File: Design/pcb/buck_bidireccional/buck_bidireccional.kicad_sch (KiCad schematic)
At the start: 19 parts, among them J1 Conn_01x02_Pin, J2 Screw_Terminal_01x02, J3 Screw_Terminal_01x02, J4 Conn_01x02_Pin, Q1 NMOS, Q2 NMOS, U1 IR2184

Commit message: updated pcb
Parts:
- removed C1: 6.8u, Capacitor_THT:CP_Radial_D5.0mm_P2.00mm, symbol Device:C
- removed C2: 2.2u, Capacitor_THT:CP_Radial_D5.0mm_P2.00mm, symbol Device:C
- added C1: 6.8u, Capacitor_THT:CP_Radial_D5.0mm_P2.00mm, symbol Device:C_Polarized
- added C2: 2.2u, Capacitor_THT:CP_Radial_D5.0mm_P2.00mm, symbol Device:C_Polarized
- added C4: 4.7u, Capacitor_THT:CP_Radial_D5.0mm_P2.00mm, symbol Device:C
- added J5: Screw_Terminal_01x02, TerminalBlock_Phoenix:TerminalBlock_Phoenix_MKDS-1,5-2-5.08_1x02_P5.08mm_Horizontal, symbol Connector:Screw_Terminal_01x02
- added R6: 10k, Resistor_THT:R_Axial_DIN0207_L6.3mm_D2.5mm_P7.62mm_Horizontal, symbol Device:R
- R4, R5: value 100k -> 10k
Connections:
- net +12V: now also J5.1 (Pin_1)
- net GND: now also C1.2, C2.2, J5.2 (Pin_2), R6.2
- net at J2.1 (Pin_1), J4.1 (Pin_1), L1.1: now also C2.1
- net at C3.2, J4.2 (Pin_2), L1.2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: now also C4.2
- net at J1.1 (Pin_1), U1.1 (IN): now also R6.1
- net at J3.1 (Pin_1), Q1.1 (D): now also C1.1
- net at D2.1 (K), R3.1, U1.7 (HO): now also C4.1

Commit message: updates kiskas
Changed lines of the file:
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@@
 (kicad_sch
-	(version 20231120)
+	(version 20250114)
 	(generator "eeschema")
-	(generator_version "8.0")
+	(generator_version "9.0")
 	(paper "A4")
+	(text_box "Footprints \n\nterminal block:	TerminalBlock_Phoenix:TerminalBlock_Phoenix_MKDS-1,5-2-5.08_1x02_P5.08mm_Horizontal \ncapacitors:  Capacitor_THT:CP_Radial_D5.0mm_P2.00mm \nresistors: R_Axial_DIN0207_L6.3mm_D2.5mm_P7.62mm_Horizontal (REVISION)\ndiodes: Diode_THT:D_A-405_P7.62mm_Horizontal(REVISION)\nmosfets: TO-220-3_Vertical\npins:	Connector_PinHeader_2.54mm:PinHeader_1x02_P2.54mm_Vertical\ndriver:	Package_DIP:DIP-8_W7.62mm"
+		(exclude_from_sim no)
+		(at 177.8 19.05 0)
+		(size 104.14 22.86)
+		(margins 0.9525 0.9525 0.9525 0.9525)
+		(stroke
+			(width 0)
+			(type default)
+		)
+		(fill
+			(type none)
+		)
+		(effects
+			(font
+				(size 1.27 1.27)
+			)
+			(justify left top)
+		)
+	)
 	(junction
 		(at 127 92.71)
@@
 			(width 0)
 			(type default)
-		)
-	)
-	(text_box "Footprints \n\nterminal block:	TerminalBlock_Phoenix:TerminalBlock_Phoenix_MKDS-1,5-2-5.08_1x02_P5.08mm_Horizontal \ncapacitors:  Capacitor_THT:CP_Radial_D5.0mm_P2.00mm \nresistors: R_Axial_DIN0207_L6.3mm_D2.5mm_P7.62mm_Horizontal (REVISION)\ndiodes: Diode_THT:D_A-405_P7.62mm_Horizontal(REVISION)\nmosfets: TO-220-3_Vertical\npins:	Connector_PinHeader_2.54mm:PinHeader_1x02_P2.54mm_Vertical\ndriver:	Package_DIP:DIP-8_W7.62mm"
-		(exclude_from_sim no)
-		(at 177.8 19.05 0)
-		(size 104.14 22.86)
-		(stroke
-			(width 0)
-			(type default)
-		)
-		(fill
-			(type none)
-		)
-		(effects
-			(font
-				(size 1.27 1.27)
-			)
-			(justify left top)
 		)
 	)
@@
 		)
 	)
+	(embedded_fonts no)
 )

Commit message: update kicad
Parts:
- C4: value 4.7u -> 100n
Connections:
- net +12V: now also C4.1
- net GND: now also C4.2
- net at C3.2, J4.2 (Pin_2), L1.2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: no longer C4.2
- net at D2.1 (K), R3.1, U1.7 (HO): no longer C4.1
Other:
- moved on the sheet: J5

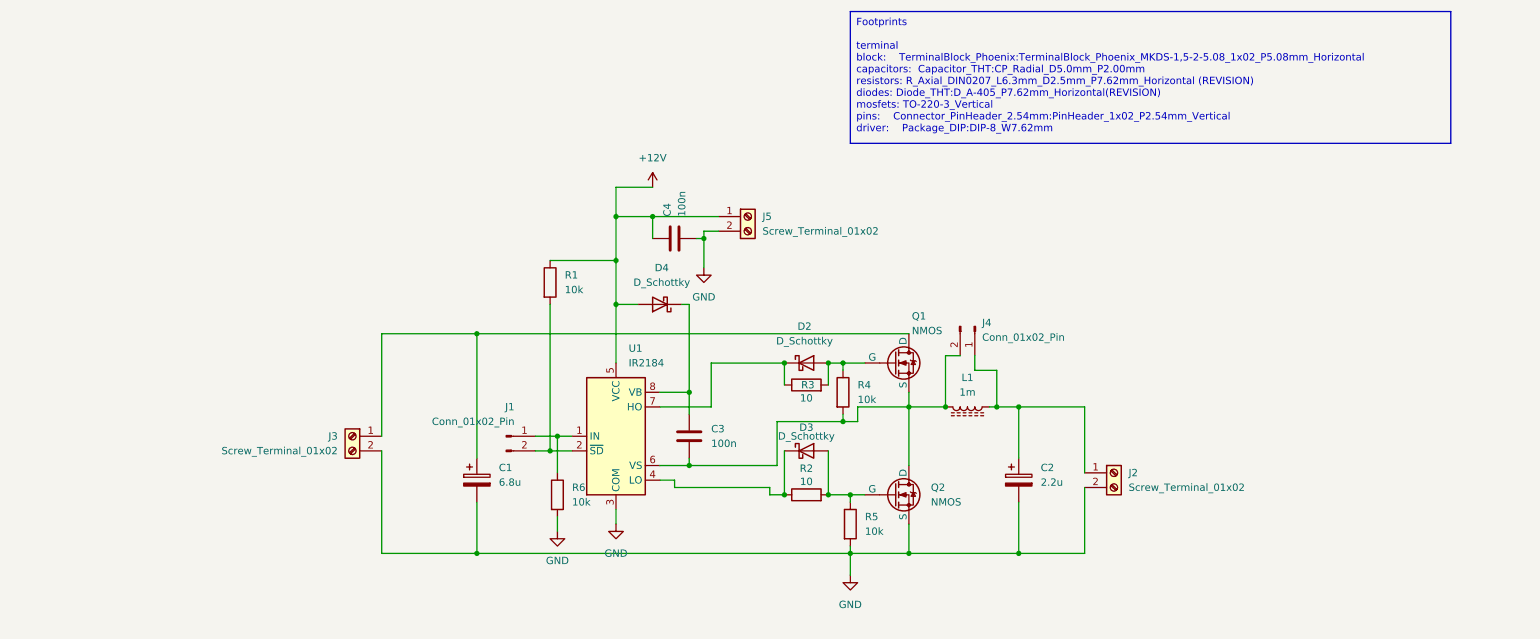
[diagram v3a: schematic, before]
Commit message: updated kicad
MOSFET gate oscilloscope reading still missing
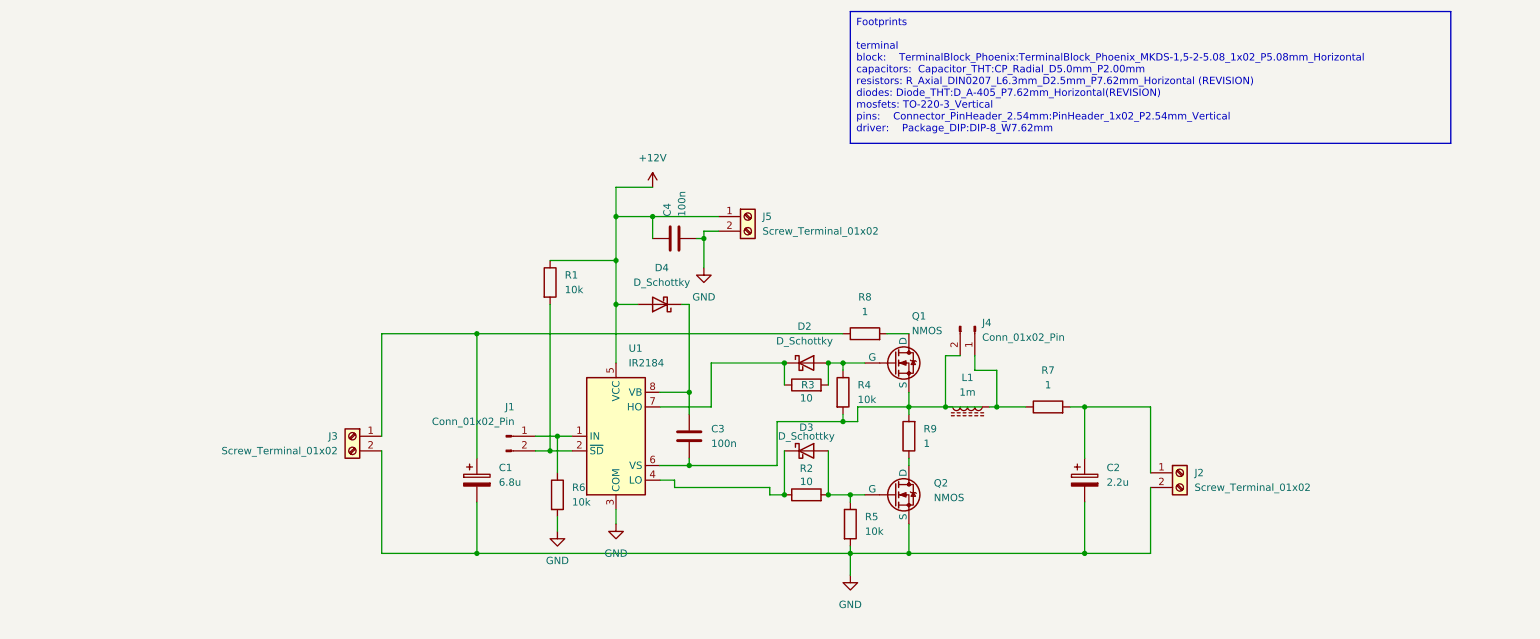
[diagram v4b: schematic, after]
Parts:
- added R7, R8, R9: 1, Resistor_THT:R_Axial_DIN0207_L6.3mm_D2.5mm_P7.62mm_Horizontal, symbol Device:R
- U1: footprint Package_DIP:DIP-8_W7.62mm -> Package_SO:SOIC-8_3.9x4.9mm_P1.27mm
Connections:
- net at J4.1 (Pin_1), L1.1: now also R7.1; no longer C2.1, J2.1 (Pin_1)
- net at C3.2, J4.2 (Pin_2), L1.2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: now also R9.2; no longer Q2.1 (D)
- net at C1.1, J3.1 (Pin_1): now also R8.1; no longer Q1.1 (D)
- new net: Q2.1 (D), R9.1
- new net: C2.1, J2.1 (Pin_1), R7.2
- new net: Q1.1 (D), R8.2
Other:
- moved on the sheet: C2, J2

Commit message: final kicad
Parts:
- removed R7, R8, R9: 1, Resistor_THT:R_Axial_DIN0207_L6.3mm_D2.5mm_P7.62mm_Horizontal, symbol Device:R
- added DQ1, DQ2, IL1: TestPoint, TestPoint:TestPoint_Bridge_Pitch2.54mm_Drill0.7mm, symbol Connector:TestPoint
- added Vgs_Q1, Vgs_Q2: Conn_01x02_Pin, Connector_PinHeader_2.54mm:PinHeader_1x02_P2.54mm_Vertical, symbol Connector:Conn_01x02_Pin
- renumbered J1 to PWM1, J5 to Vcc1, J4 to Vl1
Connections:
- net GND: now also Vgs_Q2.1 (Pin_1)
- net at L1.1, Vl1.1 (Pin_1): now also C2.1, J2.1 (Pin_1), IL1.1
- net VS: now reaches C3.2, L1.2, Q1.3 (S), R4.2, U1.6 (VS), Vl1.2 (Pin_2)
- net VS: now also Q2.1 (D), DQ2.1, Vgs_Q1.1 (Pin_1)
- net LO: now reaches D3.2 (A), Q2.2 (G), R2.2, R5.1
- net LO: now also Vgs_Q2.2 (Pin_2)
- net HO: now reaches D2.2 (A), Q1.2 (G), R3.2, R4.1
- net HO: now also Vgs_Q1.2 (Pin_2)
- net at C1.1, J3.1 (Pin_1): now also Q1.1 (D), DQ1.1
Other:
- moved on the sheet: C1, C2, C3, C4, D2, D3, D4, J2, J3, L1, PWM1, Q1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

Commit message: final pcb
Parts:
- L1: footprint BUCK_INDUCTOR:buck_inductor -> inductores:buck_inductor
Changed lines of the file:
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@@
 	)
 	(junction
-		(at 81.28 68.58)
+		(at 184.15 88.9)
 		(diameter 0)
 		(color 0 0 0 0)
 	)
 	(junction
-		(at 184.15 88.9)
+		(at 81.28 68.58)
 		(diameter 0)
 		(color 0 0 0 0)
@@
 	(wire
 		(pts
-			(xy 207.01 88.9) (xy 200.66 88.9)
-		)
-		(stroke
-			(width 0)
-			(type default)
-		)
-	)
-	(wire
-		(pts
 			(xy 184.15 104.14) (xy 184.15 105.41)
 		)
@@
 	(wire
 		(pts
-			(xy 236.22 102.87) (xy 236.22 114.3)
+			(xy 81.28 69.85) (xy 81.28 68.58)
 		)
 		(stroke
@@
 	(wire
 		(pts
-			(xy 184.15 72.39) (xy 184.15 78.74)
+			(xy 236.22 102.87) (xy 236.22 114.3)
 		)
 		(stroke
@@
 	(wire
 		(pts
-			(xy 184.15 104.14) (xy 186.69 104.14)
+			(xy 184.15 72.39) (xy 184.15 78.74)
 		)
 		(stroke
@@
 	(wire
 		(pts
-			(xy 224.79 105.41) (xy 224.79 114.3)
+			(xy 184.15 104.14) (xy 186.69 104.14)
 		)
 		(stroke
@@
 	(wire
 		(pts
-			(xy 66.04 118.11) (xy 66.04 115.57)
+			(xy 224.79 105.41) (xy 224.79 114.3)
 		)
 		(stroke
@@
 	(wire
 		(pts
-			(xy 92.71 95.25) (xy 92.71 92.71)
+			(xy 66.04 118.11) (xy 66.04 115.57)
 		)
 		(stroke
@@
 	(wire
 		(pts
-			(xy 78.74 99.06) (xy 78.74 95.25)
+			(xy 92.71 95.25) (xy 92.71 92.71)
 		)
 		(stroke
@@
 	(wire
 		(pts
-			(xy 81.28 73.66) (xy 81.28 68.58)
+			(xy 78.74 99.06) (xy 78.74 95.25)
 		)
 		(stroke
@@
 			)
 		)
-		(property "Footprint" "BUCK_INDUCTOR:buck_inductor"
+		(property "Footprint" "inductores:buck_inductor"
 			(at 204.47 88.9 0)
 			(effects
@@
 	(symbol
 		(lib_id "power:GND")
-		(at 81.28 73.66 0)
+		(at 66.04 118.11 0)
 		(unit 1)
 		(exclude_from_sim no)
@@
 		(dnp no)
 		(fields_autoplaced yes)
-		(property "Reference" "#PWR05"
-			(at 81.28 80.01 0)
+		(property "Reference" "#PWR02"
+			(at 66.04 124.46 0)
 			(effects
 				(font
@@
 		)
 		(property "Value" "GND"
-			(at 81.28 78.74 0)
+			(at 66.04 123.19 0)
 			(effects
 				(font
@@
 		)
 		(property "Footprint" ""
-			(at 81.28 73.66 0)
+			(at 66.04 118.11 0)
 			(effects
 				(font
@@
 		)
 		(property "Datasheet" ""
-			(at 81.28 73.66 0)
+			(at 66.04 118.11 0)
 			(effects
 				(font
@@
 		)
 		(property "Description" "Power symbol creates a global label with name \"GND\" , ground"
-			(at 81.28 73.66 0)
+			(at 66.04 118.11 0)
 			(effects
 				(font
@@
 			(project "buck_bidireccional"
 				(path "/a506e00b-eae2-41ca-a9b6-22a3d546bb26"
-					(reference "#PWR05")
+					(reference "#PWR02")
 					(unit 1)
 				)
@@
 	(symbol
 		(lib_id "power:GND")
-		(at 66.04 118.11 0)
+		(at 81.28 69.85 0)
 		(unit 1)
 		(exclude_from_sim no)
@@
 		(dnp no)
 		(fields_autoplaced yes)
-		(property "Reference" "#PWR02"
-			(at 66.04 124.46 0)
+		(property "Reference" "#PWR05"
+			(at 81.28 76.2 0)
 			(effects
 				(font
@@
 		)
 		(property "Value" "GND"
-			(at 66.04 123.19 0)
+			(at 81.28 74.93 0)
 			(effects
 				(font
@@
 		)
 		(property "Footprint" ""
-			(at 66.04 118.11 0)
+			(at 81.28 69.85 0)
 			(effects
 				(font
@@
 		)
 		(property "Datasheet" ""
-			(at 66.04 118.11 0)
+			(at 81.28 69.85 0)
 			(effects
 				(font
@@
 		)
 		(property "Description" "Power symbol creates a global label with name \"GND\" , ground"
-			(at 66.04 118.11 0)
+			(at 81.28 69.85 0)
 			(effects
 				(font
@@
 			(project "buck_bidireccional"
 				(path "/a506e00b-eae2-41ca-a9b6-22a3d546bb26"
-					(reference "#PWR02")
+					(reference "#PWR05")
 					(unit 1)
 				)

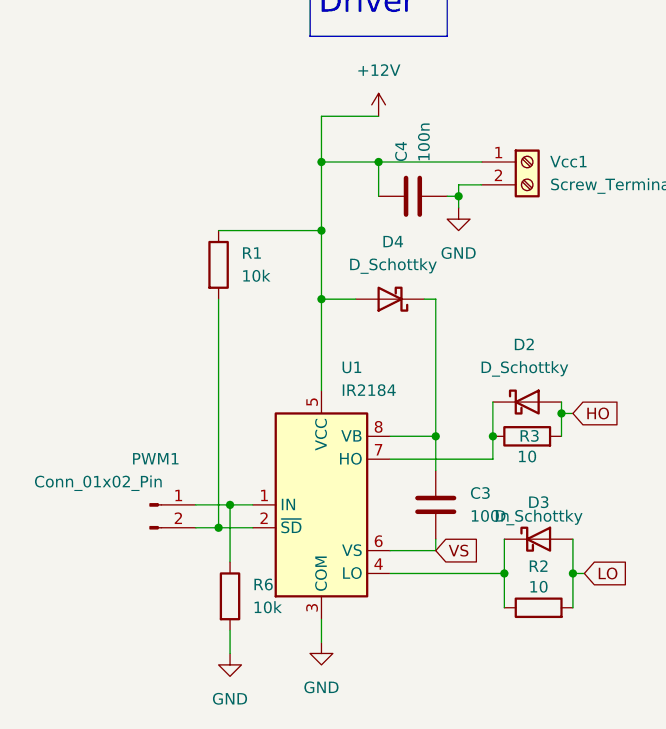
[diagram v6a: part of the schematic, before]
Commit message: removed non needed resistors
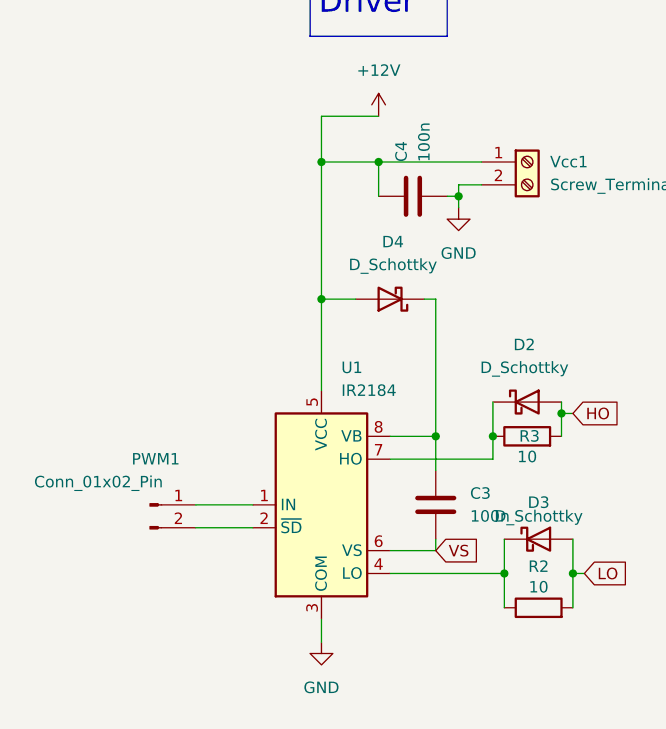
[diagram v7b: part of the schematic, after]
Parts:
- removed R1, R6: 10k, Resistor_THT:R_Axial_DIN0207_L6.3mm_D2.5mm_P7.62mm_Horizontal, symbol Device:R

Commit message: fixed kicad error
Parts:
- removed Vgs_Q1: Conn_01x02_Pin, Connector_PinHeader_2.54mm:PinHeader_1x02_P2.54mm_Vertical, symbol Connector:Conn_01x02_Pin
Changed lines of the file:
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@@
-	)
-	(junction
-		(at 189.23 88.9)
-		(diameter 0)
-		(color 0 0 0 0)
 	)
 	(junction
@@
 	)
 	(junction
-		(at 186.69 72.39)
-		(diameter 0)
-		(color 0 0 0 0)
-	)
-	(junction
 		(at 154.94 76.2)
 		(diameter 0)
@@
 	(wire
 		(pts
-			(xy 189.23 63.5) (xy 189.23 88.9)
-		)
-		(stroke
-			(width 0)
-			(type default)
-		)
-	)
-	(wire
-		(pts
 			(xy 73.66 110.49) (xy 86.36 110.49)
 		)
@@
 	(wire
 		(pts
-			(xy 184.15 88.9) (xy 189.23 88.9)
+			(xy 184.15 88.9) (xy 194.31 88.9)
 		)
 		(stroke
@@
 	(wire
 		(pts
-			(xy 189.23 88.9) (xy 194.31 88.9)
-		)
-		(stroke
-			(width 0)
-			(type default)
-		)
-	)
-	(wire
-		(pts
 			(xy 66.04 64.77) (xy 72.39 64.77)
 		)
@@
 		(pts
 			(xy 184.15 113.03) (xy 184.15 114.3)
-		)
-		(stroke
-			(width 0)
-			(type default)
-		)
-	)
-	(wire
-		(pts
-			(xy 186.69 63.5) (xy 186.69 72.39)
 		)
 		(stroke
@@
 					(unit 1)
 				)
-			)
-		)
-	)
-	(symbol
-		(lib_id "Connector:Conn_01x02_Pin")
-		(at 189.23 58.42 270)
-		(unit 1)
-		(exclude_from_sim no)
-		(in_bom yes)
-		(on_board yes)
-		(dnp no)
-		(property "Reference" "Vgs_Q1"
-			(at 177.038 62.23 90)
-			(effects
-				(font
-					(size 1.27 1.27)
-				)
-				(justify left)
-			)
-		)
-		(property "Value" "Conn_01x02_Pin"
-			(at 181.864 55.626 90)
-			(effects
-				(font
-					(size 1.27 1.27)
-				)
-				(justify left)
-			)
-		)
-		(property "Footprint" "Connector_PinHeader_2.54mm:PinHeader_1x02_P2.54mm_Vertical"
-			(at 189.23 58.42 0)
-			(effects
-				(font
-					(size 1.27 1.27)
-				)
-				(hide yes)
-			)
-		)
-		(property "Datasheet" "~"
-			(at 189.23 58.42 0)
-			(effects
-				(font
-					(size 1.27 1.27)
-				)
-				(hide yes)
-			)
-		)
-		(property "Description" "Generic connector, single row, 01x02, script generated"
-			(at 189.23 58.42 0)
-			(effects
-				(font
-					(size 1.27 1.27)
-				)
-				(hide yes)
-			)
-		)
-		(pin "1"
-		)
-		(pin "2"
-		)
-		(instances
-			(project "buck_bidireccional"
-				(path "/a506e00b-eae2-41ca-a9b6-22a3d546bb26"
-					(reference "Vgs_Q1")
-					(unit 1)
-				)
